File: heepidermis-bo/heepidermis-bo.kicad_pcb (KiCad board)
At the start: 4 copper layers, 85.7 x 54 mm, 32 parts, among them J1 Conn_01x03, J10 Conn_Boaxial, J11 Conn_Boaxial, J12 Conn_01x03, J13 Conn_01x03, J14 Conn_01x03, J15 Conn_02x16_Odd_Even, J17 Conn_02x10_Odd_Even, J18 Conn_01x03, J19 Conn_01x03, J2 Conn_02x16_Odd_Even, J20 Conn_01x03, J21 Conn_01x03, J22 Conn_01x03, J3 Conn_02x16_Odd_Even, J4 Conn_02x16_Odd_Even, J5 Conn_01x03, J6 Conn_01x03, J7 Conn_01x03, J8 Conn_01x03, J9 Conn_Boaxial

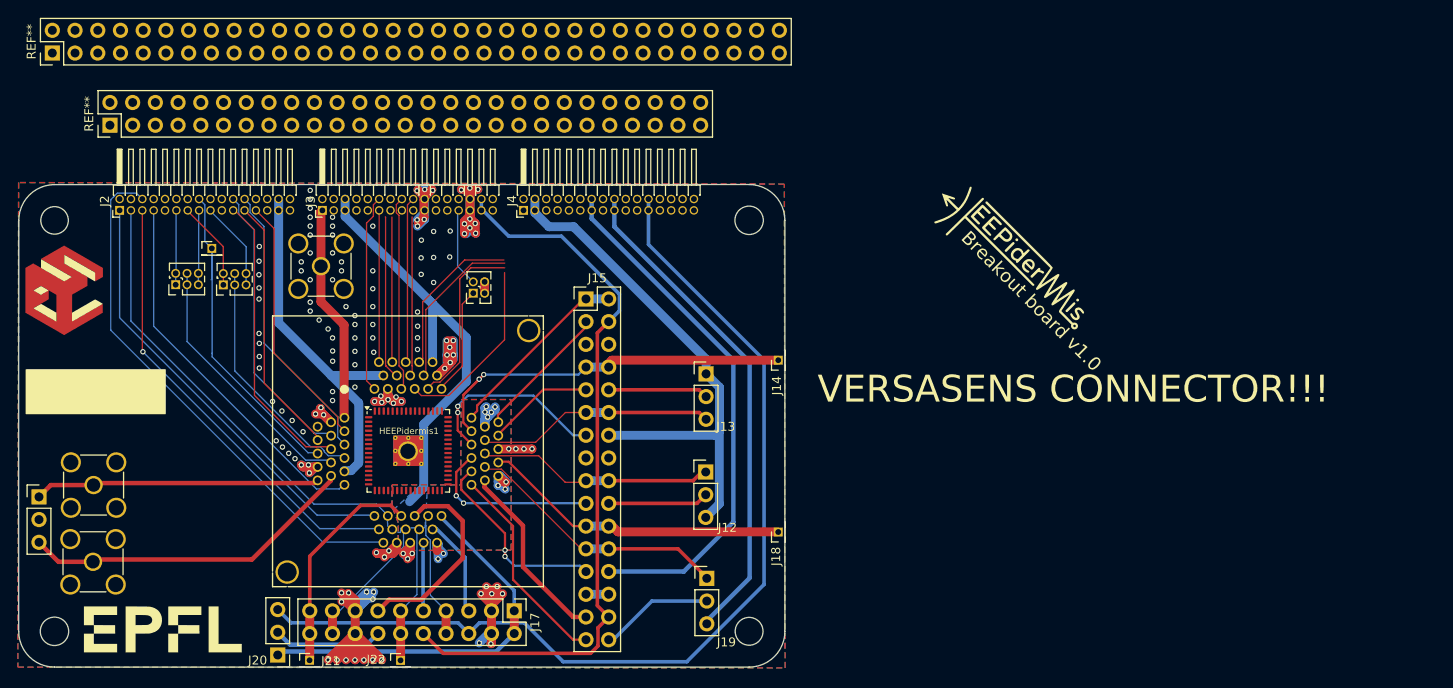
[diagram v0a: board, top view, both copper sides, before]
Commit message: Finished adding the large connector. Missing gpios and qfn footprint
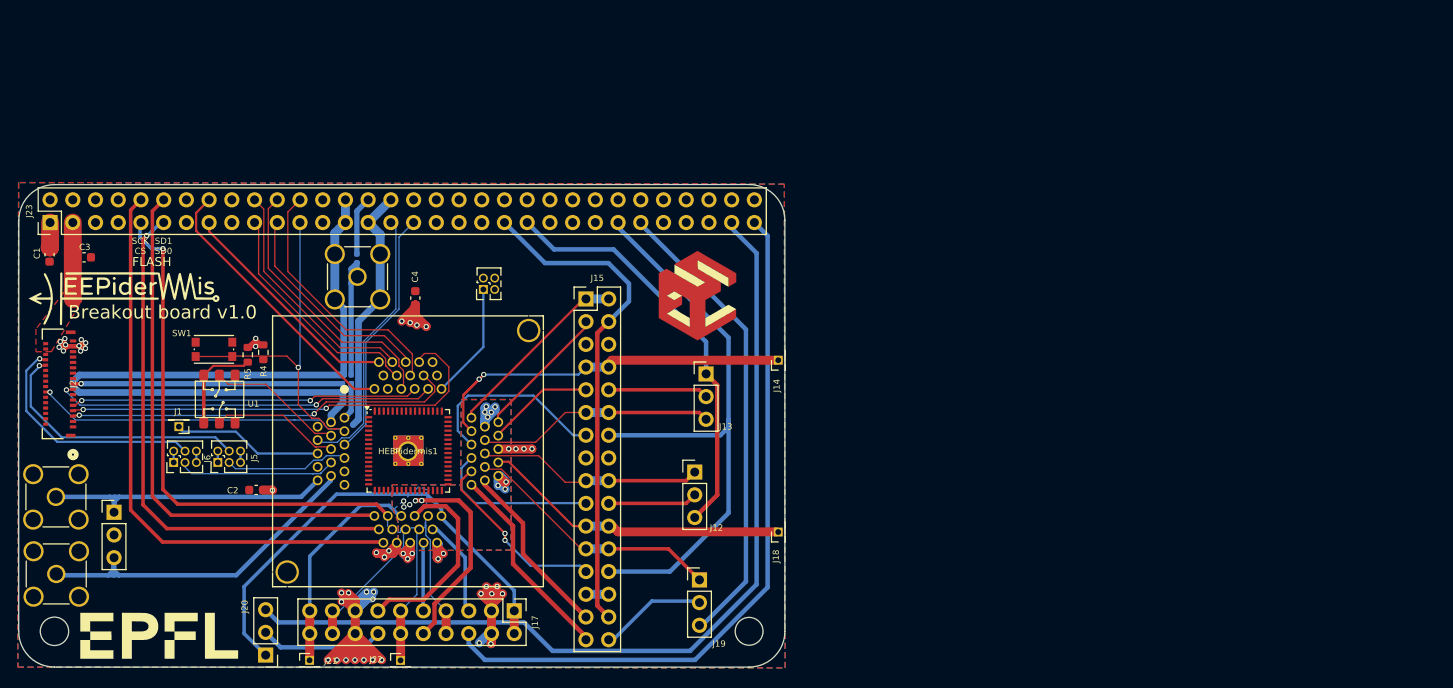
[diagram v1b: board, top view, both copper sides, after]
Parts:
- removed J3, J4: Conn_02x16_Odd_Even, Connector_PinHeader_1.27mm:PinHeader_2x16_P1.27mm_Horizontal
- removed the REF** at (103.6, 64.2)
- removed the REF** at (97.2, 56.1)
- added C1: 100n, Capacitor_SMD:C_0603_1608Metric, F.Cu at (96.9, 78.7)
- added C2: 100n, Capacitor_SMD:C_0603_1608Metric, F.Cu at (120.0, 105.0)
- added C3: 100n, Capacitor_SMD:C_0603_1608Metric, F.Cu at (100.7, 79.0)
- added C4: 100n, Capacitor_SMD:C_0603_1608Metric, F.Cu at (137.8, 83.5)
- added J23: Conn_02x29_Top_Bottom, Connector_PinHeader_2.54mm:PinHeader_2x32_P2.54mm_Vertical, F.Cu at (96.9, 75.1)
- added R1: 0R, X-MODs_PcbLib:R0402, B.Cu at (130.1, 93.1)
- added R2: 0R, X-MODs_PcbLib:R0402, B.Cu at (130.6, 92.6)
- added R3: 0R, X-MODs_PcbLib:R0402, B.Cu at (131.2, 79.1)
- added R4: 1k, Resistor_SMD:R_0603_1608Metric, F.Cu at (120.8, 89.6)
- added R5: 10k, Resistor_SMD:R_0603_1608Metric, F.Cu at (119.0, 89.9)
- added SW1: SW_Push, Button_Switch_SMD:SW_Push_1P1T_NO_CK_KMR2, F.Cu at (115.2, 89.3)
- added U1: ~, heep_footprints:SPDT-2pos-CAS-D20B1, F.Cu at (115.8, 94.8)
- J2: value Conn_02x16_Odd_Even -> 5025983393; footprint Connector_PinHeader_1.27mm:PinHeader_2x16_P1.27mm_Horizontal -> heep_footprints:CONN_502598-3393_MOL
- moved G*** 99.3 mm to (104.9, 83.4), turned to 0 degrees
- moved REF** 70.8 mm to (169.4, 88.2)
- moved J2 20.5 mm to (98.0, 93.1)
- moved J1 20.3 mm to (111.3, 97.9), turned to 180 degrees
- moved J6 19.9 mm to (110.7, 101.9)
- moved J5 19.9 mm to (115.7, 101.9)
- moved J7 8.56 mm to (104.1, 107.5)
- moved G*** 6.63 mm to (112.3, 88.9)
- moved G*** 6.63 mm to (114.1, 80.3)
- moved J10 4.41 mm to (97.6, 105.8)
- moved J9 4.33 mm to (97.6, 114.4)
- moved J11 4.25 mm to (131.3, 81.2)
- moved J20 1.35 mm to (121.0, 123.5)
- moved J12 1.23 mm to (169.0, 103.0)
- moved J8 1.21 mm to (145.4, 82.6)
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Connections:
- net /DSM_CLK renamed /DSM_CLK_GPIO_4
- net /DSM_IN renamed /DSM_IN_GPIO_5
- HEEPidermis1 pad 10: /LC_DIR -> /LC_DIR_GPIO_2
- HEEPidermis1 pad 11: /LC_XING -> /LC_XING_GPIO_3
- HEEPidermis1 pad 12: /ACORE_VSS -> GND
- HEEPidermis1 pad 13: /IO_VDD -> /SUPPLY_IO_VDD
- HEEPidermis1 pad 16: /SPI_FLASH.CS1 -> /GPIO_6
- HEEPidermis1 pad 2: /ACORE_VSS -> GND
- HEEPidermis1 pad 21: /DCORE_VDD -> /SUPPLY_DCORE_VDD
- HEEPidermis1 pad 22: /ACORE_VSS -> GND
- HEEPidermis1 pad 25: /ACORE_VSS -> GND
- HEEPidermis1 pad 31: /ACORE_VSS -> GND
- HEEPidermis1 pad 35: /ACORE_VSS -> GND
- HEEPidermis1 pad 41: /ACORE_VSS -> GND
- HEEPidermis1 pad 46: /ACORE_VSS -> GND
- HEEPidermis1 pad 50: /ACORE_VSS -> GND
- HEEPidermis1 pad 51: /DCORE_VDD -> /SUPPLY_DCORE_VDD
- HEEPidermis1 pad 61: /ACORE_VSS -> GND
- HEEPidermis1 pad 62: /IO_VDD -> /SUPPLY_IO_VDD
- HEEPidermis1 pad 9: /GPIO_5 -> /VCO_CNT_OVF
- J1 pad 1: /GPIO_5 -> /VCO_CNT_OVF
- J10 pad 2: /ACORE_VSS -> GND
- J11 pad 1: /CLOCK -> /CLOCK_coaxial
- J11 pad 2: /ACORE_VSS -> GND
- J12 pad 3: /Vout_A_7 -> /SUPPLY_IREF
- J13 pad 1: /Vout_A_7 -> /SUPPLY_IREF
- J15 pad 14: /Vout_A_7 -> /SUPPLY_REF_VDD
- J15 pad 15: /ACORE_VSS -> /GND
- J15 pad 16: /ACORE_VSS -> /GND
- J15 pad 26: /Vout_A_9 -> /SUPPLY_REF_VDD
- J15 pad 27: /ACORE_VSS -> /GND
- J15 pad 28: /ACORE_VSS -> /GND
- J15 pad 30: /Vout_A_6 -> /SUPPLY_ACORE_VDD
- J15 pad 4: /Vout_A_6 -> /SUPPLY_ACORE_VDD
- J15 pad 5: /ACORE_VSS -> /GND
- J15 pad 6: /ACORE_VSS -> /GND
- J17 pad 10: /Vout_A_6 -> /SUPPLY_DCORE_VDD
- J17 pad 15: /ACORE_VSS -> GND
- J17 pad 16: /ACORE_VSS -> GND
- J17 pad 3: /ACORE_VSS -> GND
- J17 pad 4: /ACORE_VSS -> GND
- J17 pad 6: /Vout_A_11 -> /SUPPLY_LDO_VDD
- J19 pad 3: /Vout_A_10 -> /SUPPLY_LDO_REF
- J2 pad 1: /SPI_FLASH.SD1 -> unconnected-(J2-Pad1)
- J2 pad 10: /ACORE_VSS -> unconnected-(J2-Pad10)
- J2 pad 11: /GPIO_8 -> unconnected-(J2-Pad11)
- J2 pad 12: /GPIO_9 -> unconnected-(J2-Pad12)
- J2 pad 13: /GPIO_6 -> unconnected-(J2-Pad13)
- J2 pad 14: /GPIO_7 -> /nRST
- J2 pad 15: /GPIO.LED_B_1 -> /SPI_S_CS
- J2 pad 16: /GPIO_5 -> unconnected-(J2-Pad16)
- J2 pad 17: /GPIO.LED_R_1 -> /CLOCK_vs
- J2 pad 18: /GPIO.LED_G_1 -> unconnected-(J2-Pad18)
- J2 pad 19: /ACORE_VSS -> unconnected-(J2-Pad19)
- J2 pad 2: /SPI_FLASH.SD2 -> unconnected-(J2-Pad2)
- J2 pad 20: /ACORE_VSS -> unconnected-(J2-Pad20)
- J2 pad 21: /BOOT_SEL -> unconnected-(J2-Pad21)
- J2 pad 22: /EXEC_FLASH -> unconnected-(J2-Pad22)
- J2 pad 23: /EXIT_VALID -> unconnected-(J2-Pad23)
- J2 pad 24: /EXIT_VALUE -> /LC_DIR_GPIO_2
- J2 pad 25: /nRST -> unconnected-(J2-Pad25)
- J2 pad 26: unconnected-(J2-Pin_26-Pad26) -> /LC_XING_GPIO_3
- J2 pad 27: /ACORE_VSS -> unconnected-(J2-Pad27)
- J2 pad 28: /ACORE_VSS -> unconnected-(J2-Pad28)
- J2 pad 29: /IO_VDD -> unconnected-(J2-Pad29)
- J2 pad 3: /SPI_FLASH.CS0 -> unconnected-(J2-Pad3)
- J2 pad 30: /IO_VDD -> /SUPPLY_DCORE_VDD
- J2 pad 31: /Vout_B_4 -> /SUPPLY_IO_VDD
- J2 pad 32: /Vout_diff_4 -> unconnected-(J2-Pad32)
- J2 pad 4: /SPI_FLASH.SD3 -> unconnected-(J2-Pad4)
- J2 pad 5: /SPI_FLASH.SD0 -> /SPI_S_SCK
- J2 pad 6: /SPI_FLASH.SCK -> unconnected-(J2-Pad6)
- J2 pad 7: /SPI_FLASH.CS1 -> /SPI_S_MISO
- J2 pad 9: /ACORE_VSS -> /SPI_S_MOSI
- J20 pad 3: /Vout_A_11 -> /SUPPLY_VCO_VDD
- J5 pad 1: /GPIO_6 -> Net-(J5-Pin_1)
- J5 pad 2: /GPIO_6 -> Net-(J5-Pin_1)
- J5 pad 3: /LC_DIR -> /LC_DIR_GPIO_2
- J5 pad 4: /LC_DIR -> /LC_DIR_GPIO_2
- J6 pad 1: /GPIO_8 -> Net-(J6-Pin_1)
- J6 pad 2: /GPIO_8 -> Net-(J6-Pin_1)
- J6 pad 3: /LC_XING -> /LC_XING_GPIO_3
- J6 pad 4: /LC_XING -> /LC_XING_GPIO_3
- J7 pad 2: /ACORE_VSS -> GND
- J9 pad 2: /ACORE_VSS -> GND
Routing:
- net GND: track 0.00 -> 206.0 mm, vias 0 -> 40
- net /ACORE_VSS: track 170.6 -> 0.00 mm, vias 142 -> 0
- net /SUPPLY_DCORE_VDD: track 0.00 -> 122.9 mm, vias 0 -> 9
- net /SUPPLY_IO_VDD: track 0.00 -> 121.5 mm, vias 0 -> 13
- net /Vout_A_11: track 109.2 -> 0.00 mm
- net /SUPPLY_VCO_VDD: track 0.00 -> 101.9 mm
- net /Vout_A_6: track 82.6 -> 0.00 mm
- net /SUPPLY_LDO_VDD: track 0.00 -> 80.1 mm
- net /SUPPLY_REF_VDD: track 0.00 -> 68.3 mm
- net /Vout_A_7: track 59.5 -> 0.00 mm
- net /Vout_A_9: track 58.9 -> 0.00 mm
- net /SUPPLY_ACORE_VDD: track 0.00 -> 56.0 mm
- net /Vout_A_10: track 55.7 -> 0.00 mm
- net /SUPPLY_LDO_REF: track 0.00 -> 52.2 mm
- net /DCORE_VDD: track 49.4 -> 0.00 mm
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- added copper zone on B.Cu, net /SUPPLY_DCORE_VDD
- added copper zone on F.Cu, net /SUPPLY_DCORE_VDD
- added copper zone on In1.Cu, net /SUPPLY_DCORE_VDD
- added copper zone on B.Cu, net GND
- added copper zone on F.Cu, net GND
- added copper zone on In1.Cu, net GND
- added copper zone on In2.Cu, net GND
- removed copper zone on B.Cu, net /ACORE_VSS
- removed copper zone on F.Cu, net /ACORE_VSS
- removed copper zone on B.Cu, net /DCORE_VDD
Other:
- outline, holes or cut-outs redrawn
- board text added: "FLASH"
- board text added: "SCK CS"
- board text added: "SD1 SD0"
- board text removed: "VERSASENS CONNECTOR!!!"
